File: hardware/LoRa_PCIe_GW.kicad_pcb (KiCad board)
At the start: 6 copper layers, 50.9 x 30 mm, 239 parts, among them Q300 NC, Q600 NC, U100 SX1303, U201 3V3, U202 TPS62242DRV, U203 3V3, U204 STTS751, U205 NCP176BMX330TCG, U206 3V3, U300 NC, U600 ZOE-M8Q, U700 NC, U800 SX1250, U801 SAW Filter, U802 SKY66423-11, U803 SAW Filter, U805 SAW Filter, U900 SX1250, Y800 TCXO

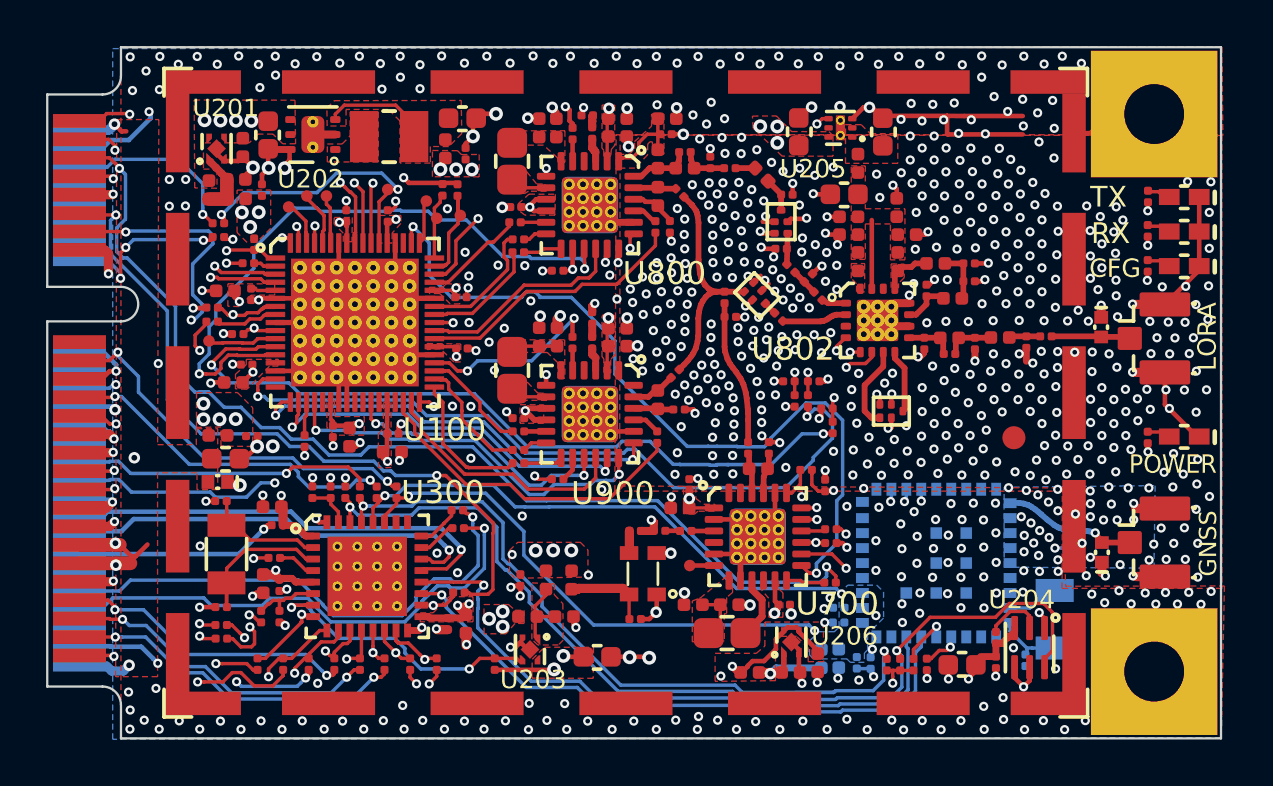
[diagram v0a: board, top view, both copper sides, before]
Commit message: Finished routing. Still needs work for DRC errors.
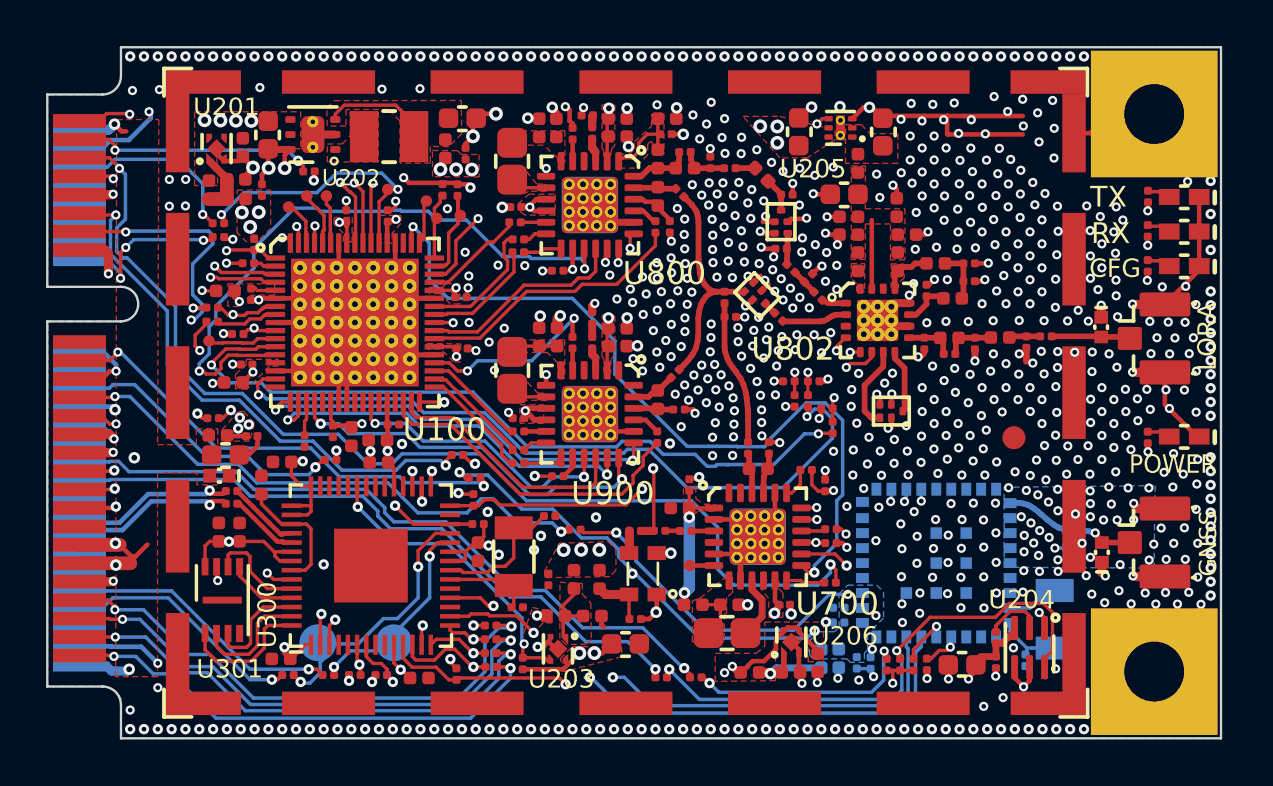
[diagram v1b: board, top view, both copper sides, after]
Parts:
- removed C301, C307, C310: NC, LoRa_PCIe_GW:rlc_402_smd_small
- removed C302, C306, C311, R303, R304, R305, R321: NC, LoRa_PCIe_GW:rlc_201_smd_small
- added C10: 0.1uF, LoRa_PCIe_GW:rlc_402_smd_small, F.Cu at (107.5, 121.0)
- added C2: 0.1uF, LoRa_PCIe_GW:rlc_402_smd_small, F.Cu at (116.2, 127.4)
- added C3: 0.1uF, LoRa_PCIe_GW:rlc_402_smd_small, F.Cu at (114.4, 118.0)
- added C4: 0.1uF, LoRa_PCIe_GW:rlc_402_smd_small, F.Cu at (108.3, 121.0)
- added C5: 0.1uF, LoRa_PCIe_GW:rlc_402_smd_small, F.Cu at (110.2, 126.5)
- added C6: 0.1uF, LoRa_PCIe_GW:rlc_402_smd_small, F.Cu at (118.7, 121.9)
- added C7: 0.1uF, LoRa_PCIe_GW:rlc_402_smd_small, F.Cu at (110.2, 118.0)
- added C8: 0.1uF, LoRa_PCIe_GW:rlc_402_smd_small, F.Cu at (109.3, 119.0)
- added R1: 10K, LoRa_PCIe_GW:rlc_201_smd_small, F.Cu at (118.7, 120.7)
- added R2: 27R, LoRa_PCIe_GW:rlc_201_smd_small, F.Cu at (108.0, 119.3)
- added R3: 27R, LoRa_PCIe_GW:rlc_201_smd_small, F.Cu at (108.0, 119.8)
- added TP10: TestPoint, nebra:TestPoint_SMD_1.6mm, B.Cu at (115.0, 125.8)
- added TP11: TestPoint, nebra:TestPoint_SMD_1.6mm, B.Cu at (111.8, 125.8)
- added U301: GD25Q16EEIGR, nebra:DFN-8-1EP_3x2mm_P0.5mm_EP0.2x1.6mm, F.Cu at (107.6, 124.0)
- U300: value NC -> RP2040; footprint LoRa_PCIe_GW:UFQFPN32_5x5mm -> nebra:QFN56_RP2040
- Y300: renamed from Q300; value NC -> 12 MHz
- moved R314 22.1 mm to (111.4, 105.4), turned to 0 degrees
- moved R308 16.6 mm to (128.2, 127.3), turned to 0 degrees
- moved R309 15.9 mm to (126.7, 127.3), turned to 0 degrees
- moved C304 14.8 mm to (121.8, 120.3), turned to 180 degrees
- moved C303 13.7 mm to (120.4, 124.3), turned to 0 degrees
- moved Y300 12.5 mm to (120.2, 122.1), turned to -90 degrees
- moved R323 9.76 mm to (110.5, 127.2), turned to 0 degrees
- moved R302 9.42 mm to (112.3, 117.9), turned to 0 degrees
- moved R322 9.08 mm to (112.2, 127.2), turned to 0 degrees
- moved R331 8.75 mm to (122.9, 120.9), turned to 180 degrees
- moved R319 7.93 mm to (119.3, 126.9), turned to 0 degrees
- moved R312 7.64 mm to (118.5, 119.7), turned to -90 degrees
- moved R306 7.53 mm to (117.8, 127.2), turned to -90 degrees
- moved R334 7.12 mm to (114.5, 127.2)
- moved R316 6.99 mm to (119.2, 125.1), turned to 0 degrees
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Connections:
- net /SCH2/DEBUG_JTCK-SWCLK renamed /SCH2/DBG_SWCLK
- net Net-(PCIe_1-Pad1) renamed /SCH2/P_SX1261_BUSY
- net Net-(PCIe_1-Pad11) renamed /SCH2/P_SX1261_NRESET
- net Net-(PCIe_1-Pad13) renamed /SCH2/P_MCU_NRESET
- net Net-(PCIe_1-Pad16) renamed /SCH2/P_POWER_EN
- net Net-(PCIe_1-Pad19) renamed /SCH2/P_PPS
- net Net-(PCIe_1-Pad22) renamed /SCH2/P_SX1302_RESET
- net Net-(PCIe_1-Pad23) renamed /SCH2/~{P_GNSS_RESET}
- net Net-(PCIe_1-Pad25) renamed /SCH2/P_GNSS_STANDBY
- net Net-(PCIe_1-Pad3) renamed /SCH2/P_SX1261_DIO1
- net Net-(PCIe_1-Pad30) renamed /SCH2/P_I2C_SCL
- net Net-(PCIe_1-Pad31) renamed /SCH2/H_UART_TX
- net Net-(PCIe_1-Pad32) renamed /SCH2/P_I2C_SDA
- net Net-(PCIe_1-Pad33) renamed /SCH2/H_UART_RX
- net Net-(PCIe_1-Pad44) renamed /SCH2/P_DBG_SWCLK
- net Net-(PCIe_1-Pad45) renamed /SCH2/P_HOST_SCK
- net Net-(PCIe_1-Pad46) renamed /SCH2/P_DBG_SWDIO
- net Net-(PCIe_1-Pad47) renamed /SCH2/P_HOST_MISO
- net Net-(PCIe_1-Pad49) renamed /SCH2/P_HOST_MOSI
- net Net-(PCIe_1-Pad5) renamed /SCH2/P_SX1261_DIO2
- net Net-(PCIe_1-Pad51) renamed /SCH2/P_HOST_CSN
- net Net-(PCIe_1-Pad6) renamed /SCH2/P_GPIO(6)
- net Net-(PCIe_1-Pad7) renamed /SCH2/P_SX1261_NSS
- C303 pad 1: /SCH2/OSC32_IN -> Net-(C303-Pad1)
- C304 pad 2: /SCH2/OSC32_OUT -> Net-(C304-Pad2)
- PCIe_1 pad 10: Net-(PCIe_1-Pad10) -> unconnected-(PCIe_1-Pad10)
- PCIe_1 pad 12: Net-(PCIe_1-Pad12) -> unconnected-(PCIe_1-Pad12)
- PCIe_1 pad 14: Net-(PCIe_1-Pad14) -> unconnected-(PCIe_1-Pad14)
- PCIe_1 pad 17: Net-(PCIe_1-Pad17) -> unconnected-(PCIe_1-Pad17)
- PCIe_1 pad 20: Net-(PCIe_1-Pad20) -> unconnected-(PCIe_1-Pad20)
- PCIe_1 pad 28: Net-(PCIe_1-Pad28) -> unconnected-(PCIe_1-Pad28)
- PCIe_1 pad 36: /SCH2/USB_DN -> /SCH2/USB_D-
- PCIe_1 pad 38: /SCH2/USB_DP -> /SCH2/USB_D+
- PCIe_1 pad 42: Net-(PCIe_1-Pad42) -> unconnected-(PCIe_1-Pad42)
- PCIe_1 pad 48: Net-(PCIe_1-Pad48) -> unconnected-(PCIe_1-Pad48)
- PCIe_1 pad 8: Net-(PCIe_1-Pad8) -> unconnected-(PCIe_1-Pad8)
- R323 pad 2: /SCH2/DEBUG_JTMS-SWDIO -> /SCH2/DBG_SWDIO
- R331 pad 1: ~GNSS_RESET~ -> ~{GNSS_RESET}
- R601 pad 1: ~GNSS_RESET~ -> ~{GNSS_RESET}
- U100 pad 17: Net-(U100-Pad17) -> unconnected-(U100-Pad17)
- U100 pad 22: Net-(U100-Pad22) -> unconnected-(U100-Pad22)
- U100 pad 26: Net-(U100-Pad26) -> unconnected-(U100-Pad26)
- U100 pad 27: Net-(U100-Pad27) -> unconnected-(U100-Pad27)
- U100 pad 29: Net-(U100-Pad29) -> unconnected-(U100-Pad29)
- U100 pad 31: Net-(U100-Pad31) -> unconnected-(U100-Pad31)
- U100 pad 54: Net-(U100-Pad54) -> unconnected-(U100-Pad54)
- U300 pad 10: HOST_CSN -> VCCIO33
- U300 pad 11: HOST_SCK -> SX1261_BUSY
- U300 pad 12: HOST_MISO -> HOST_CSN
- U300 pad 13: HOST_MOSI -> HOST_SCK
- U300 pad 14: SX1261_NSS -> HOST_MOSI
- U300 pad 15: SX1261_DIO1 -> HOST_MISO
- U300 pad 16: GND -> PPS
- U300 pad 17: VCCIO33 -> unconnected-(U300-Pad17)
- U300 pad 18: SX1261_NRESET -> ~{GNSS_RESET}
- U300 pad 19: HOST_UART_TX -> unconnected-(U300-Pad19)
- U300 pad 2: /SCH2/OSC32_IN -> I2C_SCL
- U300 pad 20: HOST_UART_RX -> Net-(C303-Pad1)
- U300 pad 21: /SCH2/USB_DN -> Net-(C304-Pad2)
- U300 pad 22: /SCH2/USB_DP -> VCCIO33
- U300 pad 23: /SCH2/DEBUG_JTMS-SWDIO -> VCCIO33
- U300 pad 25: Net-(U300-Pad25) -> /SCH2/DBG_SWDIO
- U300 pad 26: Net-(U300-Pad26) -> /SCH2/MCU_NRESET
- U300 pad 27: PPS -> unconnected-(U300-Pad27)
- U300 pad 28: ~GNSS_RESET~ -> SX1261_NSS
- U300 pad 29: I2C_SCL -> SX1261_DIO1
- U300 pad 3: /SCH2/OSC32_OUT -> I2C_SDA
- U300 pad 30: I2C_SDA -> SX1261_NRESET
- U300 pad 31: Net-(R304-Pad2) -> SX1302_RESET
- U300 pad 32: GND -> unconnected-(U300-Pad32)
- U300 pad 33: GND -> VCCIO33
- U300 pad 4: /SCH2/MCU_NRESET -> unconnected-(U300-Pad4)
- U300 pad 5: VCCIO33 -> unconnected-(U300-Pad5)
- U300 pad 6: /SCH2/RADIO_A_CLK_32M_MCU -> HOST_UART_TX
- U300 pad 7: POWER_EN -> HOST_UART_RX
- U300 pad 8: SX1302_RESET -> unconnected-(U300-Pad8)
- U300 pad 9: SX1261_BUSY -> unconnected-(U300-Pad9)
- U600 pad 12: Net-(U600-Pad12) -> unconnected-(U600-Pad12)
- U600 pad 14: ~GNSS_RESET~ -> ~{GNSS_RESET}
- U600 pad 22: Net-(U600-Pad22) -> unconnected-(U600-Pad22)
- U600 pad 23: Net-(U600-Pad23) -> unconnected-(U600-Pad23)
- U600 pad 24: Net-(U600-Pad24) -> unconnected-(U600-Pad24)
- U600 pad 25: Net-(U600-Pad25) -> unconnected-(U600-Pad25)
- U600 pad 26: Net-(U600-Pad26) -> unconnected-(U600-Pad26)
- U600 pad 27: Net-(U600-Pad27) -> unconnected-(U600-Pad27)
- U600 pad 32: Net-(U600-Pad32) -> unconnected-(U600-Pad32)
- U600 pad 33: Net-(U600-Pad33) -> unconnected-(U600-Pad33)
- U600 pad 34: Net-(U600-Pad34) -> unconnected-(U600-Pad34)
- U600 pad 35: Net-(U600-Pad35) -> unconnected-(U600-Pad35)
- U600 pad 5: Net-(U600-Pad5) -> unconnected-(U600-Pad5)
- U600 pad 6: Net-(U600-Pad6) -> unconnected-(U600-Pad6)
- U700 pad 23: Net-(U700-Pad23) -> unconnected-(U700-Pad23)
- U700 pad 24: Net-(U700-Pad24) -> unconnected-(U700-Pad24)
- U700 pad 4: Net-(U700-Pad4) -> unconnected-(U700-Pad4)
- U800 pad 4: Net-(U800-Pad4) -> unconnected-(U800-Pad4)
- U802 pad 14: Net-(U802-Pad14) -> unconnected-(U802-Pad14)
- U802 pad 3: Net-(U802-Pad3) -> unconnected-(U802-Pad3)
- U900 pad 1: Net-(U900-Pad1) -> unconnected-(U900-Pad1)
- U900 pad 24: Net-(U900-Pad24) -> unconnected-(U900-Pad24)
- U900 pad 4: Net-(U900-Pad4) -> unconnected-(U900-Pad4)
- Y300 pad 1: /SCH2/OSC32_OUT -> Net-(C304-Pad2)
- Y300 pad 2: /SCH2/OSC32_IN -> Net-(C303-Pad1)
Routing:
- net ~GNSS_RESET~: track 34.1 -> 0.00 mm, vias 3 -> 0
- net /SCH2/P_SX1261_DIO1: track 44.6 -> 10.5 mm
- net ~{GNSS_RESET}: track 0.00 -> 33.1 mm, vias 0 -> 4
- net GND: track 160.1 -> 127.3 mm, vias 745 -> 753
- net RADIO_A_CLK_32M: track 28.3 -> 1.32 mm, vias 2 -> 1
- net /SCH2/USB_DN: track 19.6 -> 0.00 mm, vias 1 -> 0
- net /SCH2/USB_DP: track 18.6 -> 0.00 mm, vias 1 -> 0
- net VCCCORE12: track 16.2 -> 34.0 mm
- net /SCH2/P_I2C_SCL: track 13.1 -> 30.6 mm
- net /SCH2/P_I2C_SDA: track 12.7 -> 28.9 mm, vias 2 -> 1
- net /SCH2/P_DBG_SWDIO: track 23.6 -> 10.6 mm
- net /SCH2/MCU_NRESET: track 1.66 -> 14.3 mm, vias 0 -> 2
- net SX1302_RESET: track 29.2 -> 17.3 mm, vias 2 -> 3
- net HOST_UART_RX: track 40.9 -> 29.4 mm
- net /SCH2/DBG_SWDIO: track 0.00 -> 11.3 mm, vias 0 -> 2
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- removed copper zone on In3.Cu, net GND
- removed copper zone on In3.Cu, net VCC3V3_IN
- removed copper zone on In3.Cu, net VCCCORE12
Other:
- net class Default removed
- net class GND removed
- net class Microstrip 50ohm removed
- net class Power Lines removed
- net class USB removed
- board text added: "NBR.PCB.002409"
- board text removed: "Rev: 1.0"

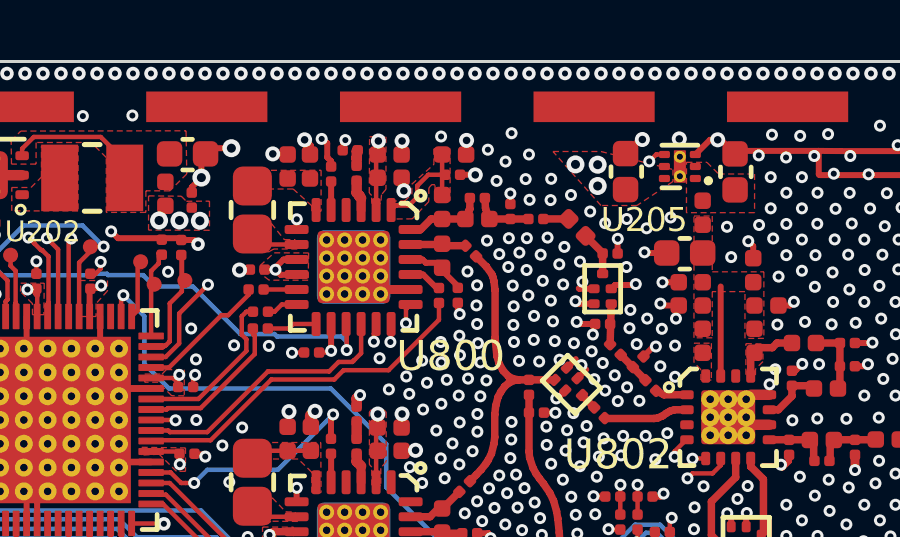
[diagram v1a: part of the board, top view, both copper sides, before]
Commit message: Fixed branding issues on the back side
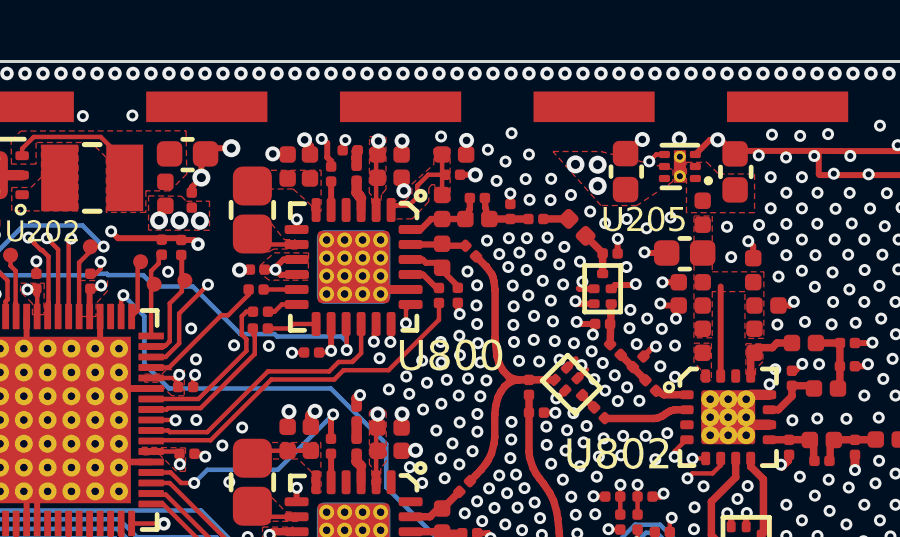
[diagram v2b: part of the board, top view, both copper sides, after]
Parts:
- moved Logo3 4.62 mm to (117.0, 107.4)
- moved Logo5 1.96 mm to (136.6, 102.2)
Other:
- board text added: "Gateway mPCIe Module for"
- board text removed: "LoRa Gateway mPCIe Module (SX1302/3)"
- board text removed: "nebra.com"

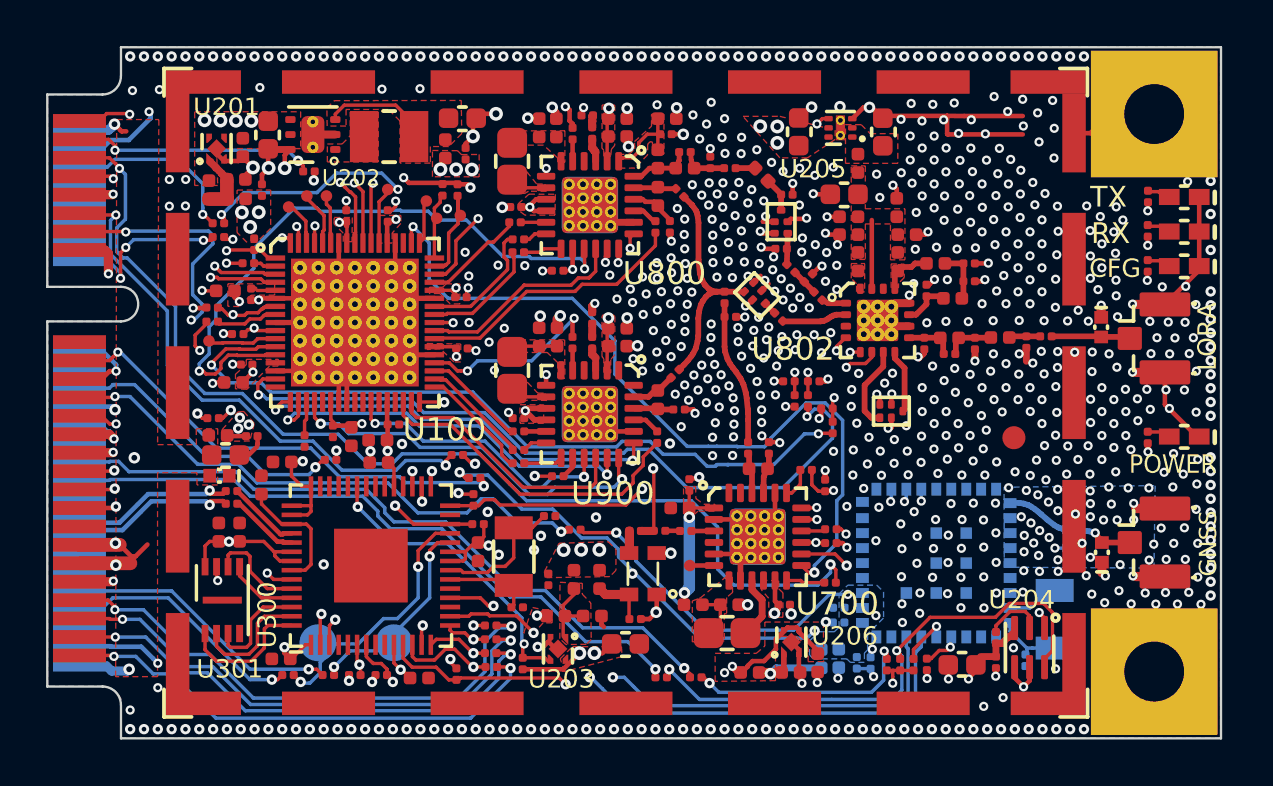
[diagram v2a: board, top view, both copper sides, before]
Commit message: Fixed DRC errors and warnings. Improved manufacturing quality.
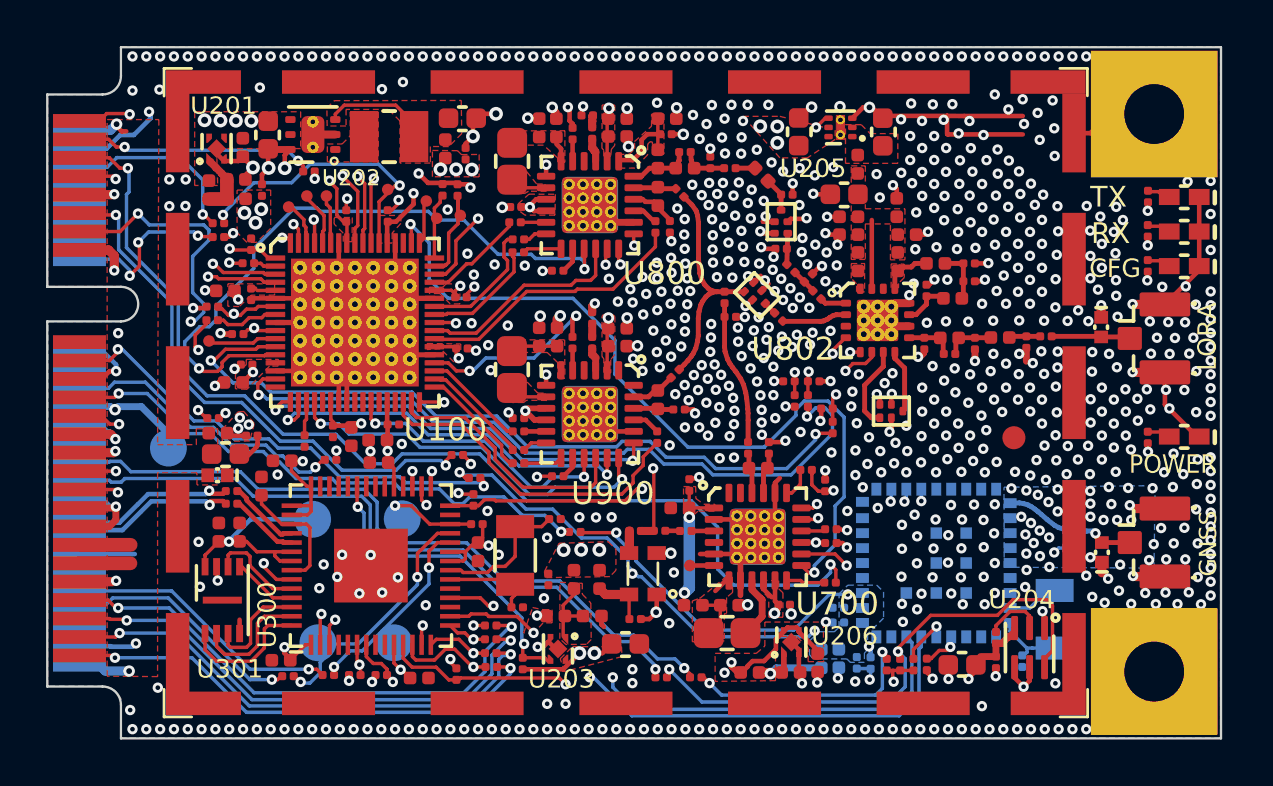
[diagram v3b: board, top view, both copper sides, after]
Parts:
- added TP12: TestPoint, nebra:TestPoint_SMD_1.6mm, B.Cu at (113.5, 122.9)
- added TP13: TestPoint, nebra:TestPoint_SMD_1.6mm, B.Cu at (111.5, 120.5)
- added TP14: TestPoint, nebra:TestPoint_SMD_1.6mm, B.Cu at (115.4, 120.5)
- added TP15: TestPoint, nebra:TestPoint_SMD_1.6mm, B.Cu at (105.3, 117.4)
- moved Logo2 1.46 mm to (107.5, 119.3)
- moved Logo1 1.46 mm to (107.5, 126.4)
- moved Logo4 1.24 mm to (119.4, 127.7)
- moved C304 0.26 mm to (122.0, 120.5)
- moved R602 0.15 mm to (142.3, 126.7)
- moved R103 0.13 mm to (108.8, 108.5)
- moved R331 0.10 mm to (122.9, 121.0)
- moved FB302 0.10 mm to (107.4, 116.8)
- moved D302 0.09 mm to (107.4, 118.6)
- moved Y300 0.08 mm to (120.3, 122.1)
- moved C809 0.07 mm to (133.4, 110.8)
- moved C5 0.06 mm to (110.2, 126.6)
- moved R108 0.06 mm to (107.2, 111.8)
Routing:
- net GND: track 127.3 -> 134.5 mm, vias 753 -> 771
- net VCCIO33: track 37.4 -> 42.3 mm
- net VCC3V3_IN: track 12.9 -> 15.3 mm, vias 6 -> 3
- net VCCCORE12: track 34.0 -> 36.4 mm
- net Net-(C601-Pad2): track 13.6 -> 14.9 mm
- net I2C_SCL: track 47.4 -> 48.6 mm
- net POWER_EN: track 30.8 -> 31.8 mm
- net HOST_SCK: track 50.9 -> 50.0 mm
- net /SCH2/P_GNSS_STANDBY: track 48.2 -> 49.1 mm
- net VDD_RADIO: track 8.25 -> 9.12 mm
- net Net-(C817-Pad2): track 0.00 -> 0.83 mm
- net RADIO_A_SCK: track 15.4 -> 16.2 mm
- net Net-(C717-Pad2): track 2.03 -> 2.79 mm
- net /SCH2/P_I2C_SDA: track 28.9 -> 29.6 mm
- net HOST_MOSI: track 53.2 -> 53.9 mm
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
